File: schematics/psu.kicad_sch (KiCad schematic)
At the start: 32 parts, among them Q1 Si9933CDY, Q2 BSS138, U10 LTC4002-ES8, U11 MAX604, U12 MAX604, U9 BQ29200

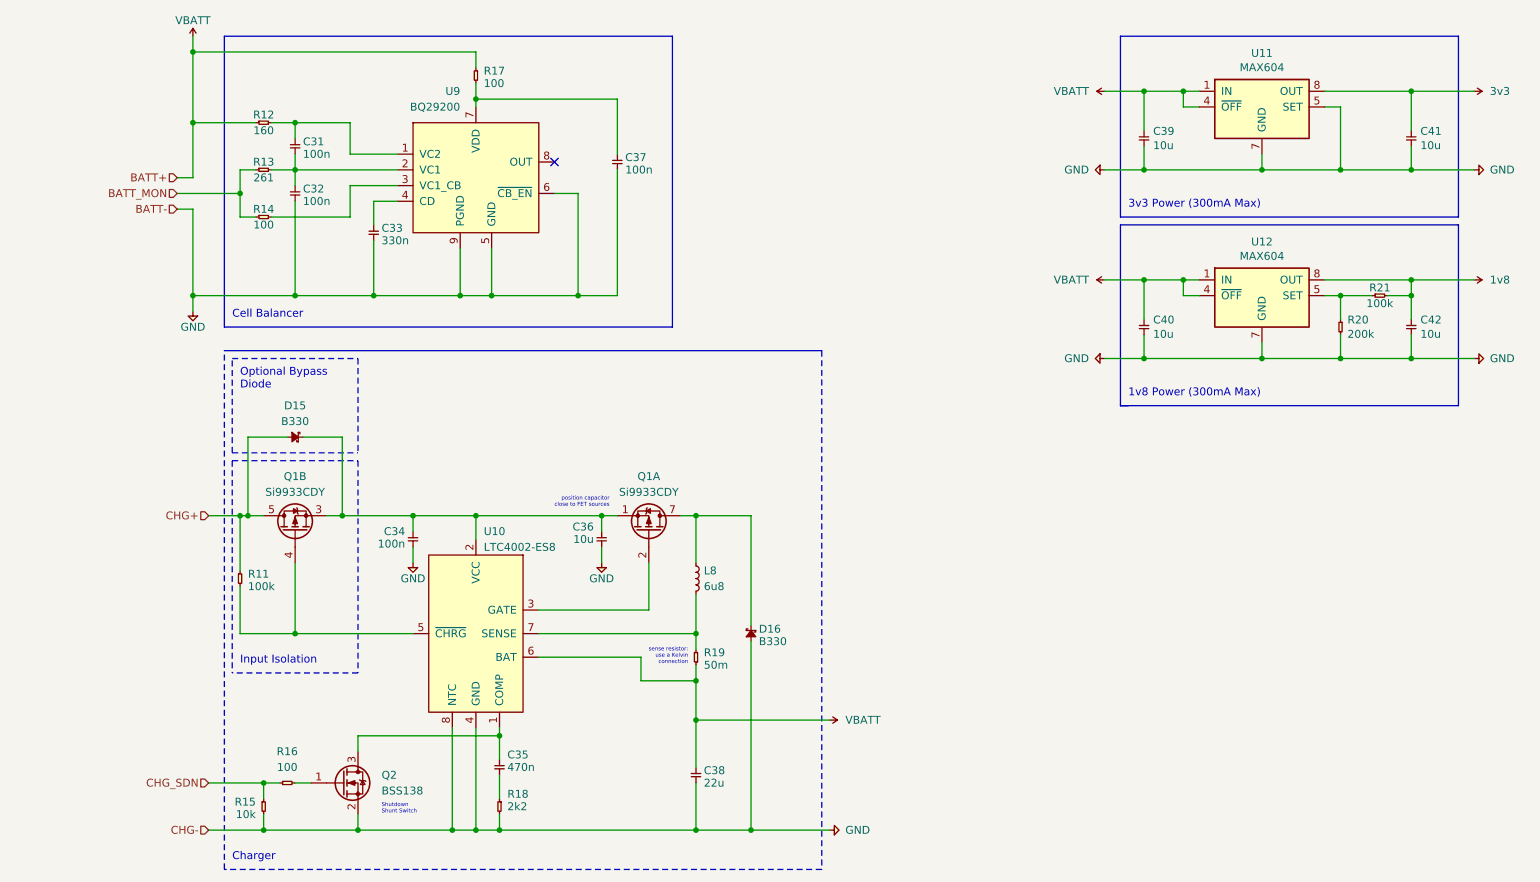
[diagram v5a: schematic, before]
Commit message: Mark isolated PGND on schematic
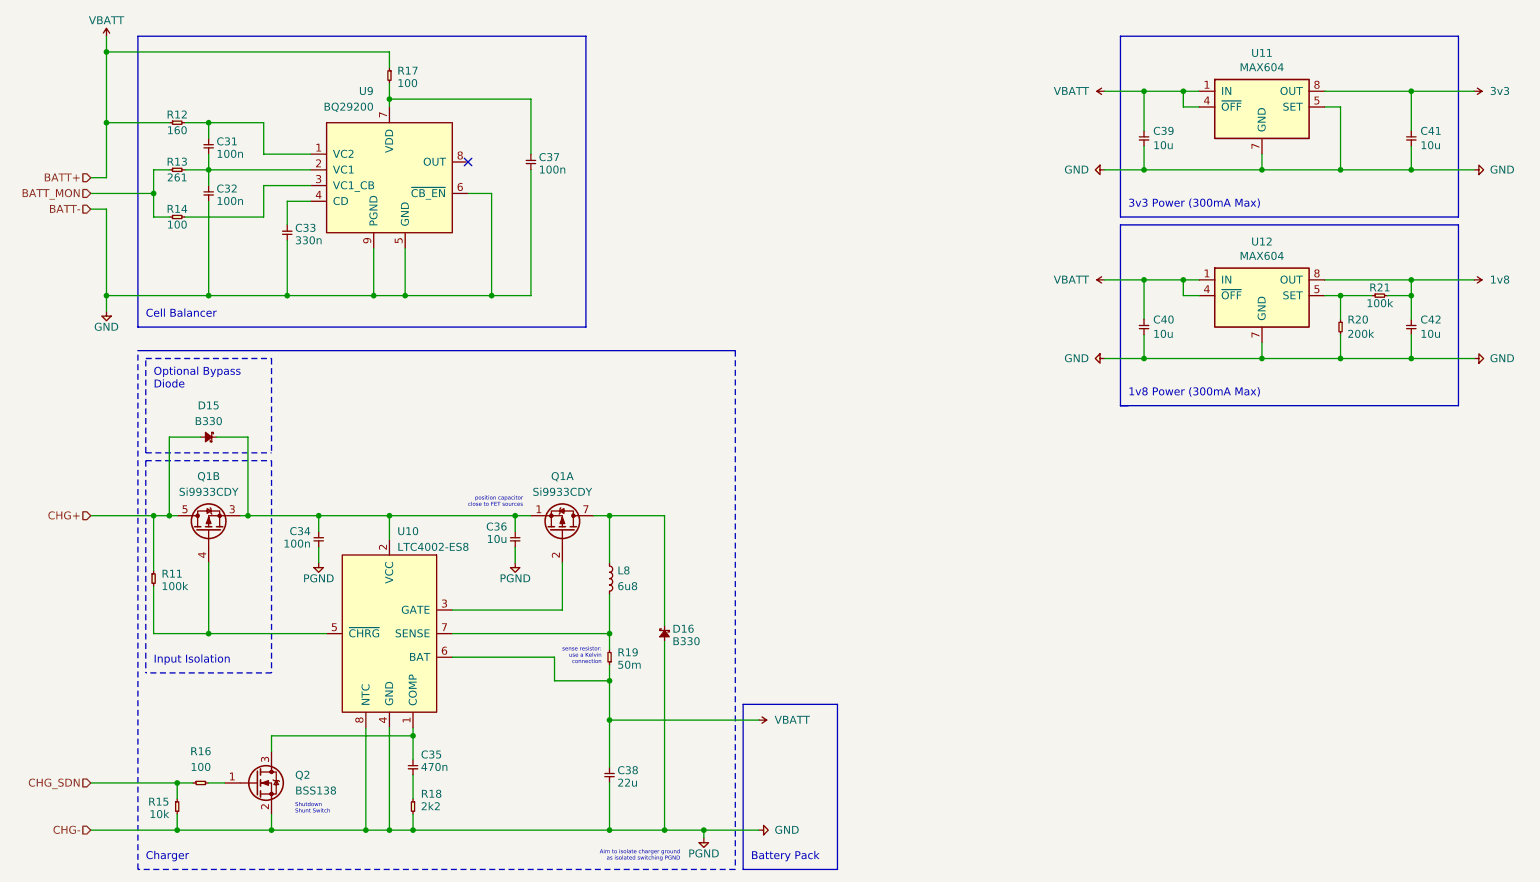
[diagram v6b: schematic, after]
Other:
- note added: "Aim to isolate charger ground as isolated switching PGND"
- note added: "Battery Pack"
- moved on the sheet: C31, C32, C33, C34, C35, C36, C37, C38, D15, D16, L8, Q1A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

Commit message: Rough power and RF layouts
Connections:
- net COMP: now reaches C35.1, Q2.3 (D), U10.1 (COMP)
- net VCC_CHG: now reaches C34.1, C36.1, D15.1, Q1.1 (S1), Q1.3 (S2), U10.2 (VCC)
- net ~{CHRG}: now reaches Q1.4 (G2), R11.2, U10.5 (~{CHRG})
- net SENSE: now reaches L8.2, R19.2, U10.7 (SENSE)
- net V_SW: now reaches D16.1, L8.1, Q1.7 (D1), Q1.8 (D1)
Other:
- note added: "Aim to isolate charger ground as isolated switching PGND through pack GND connection"
- note added: "Note the excess of labels here: this lets us create polygons instead of traces"
- note removed: "Aim to isolate charger ground as isolated switching PGND"
- moved on the sheet: R17
